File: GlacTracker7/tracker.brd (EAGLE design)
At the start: 120 x 89.3 mm, 84 parts, among them J1 THING_PLUS_PHYSICAL, Q1 2N3906, Q2 DMG6602SVT, Q3 DMG6602SVT, Q6 MMBT3906LT1SMD, Q7 DMG6602SVT, U2 FONA-800-BREAKOUT, U3 MP2155GQ-Z, U4 SPARKFUN-SWARM-M138, U5 SPARKFUN-GPS-ZED-F9P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

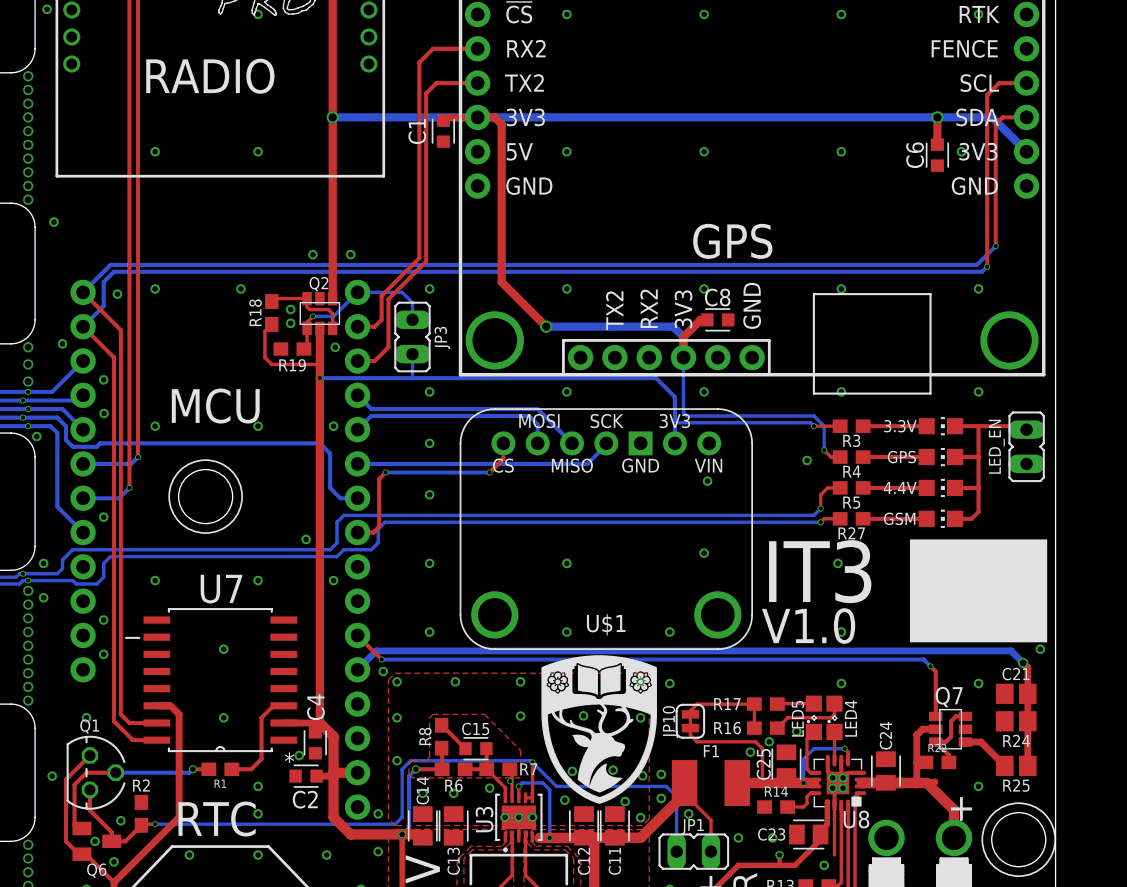
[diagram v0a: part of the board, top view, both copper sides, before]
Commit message: Added accelerometer
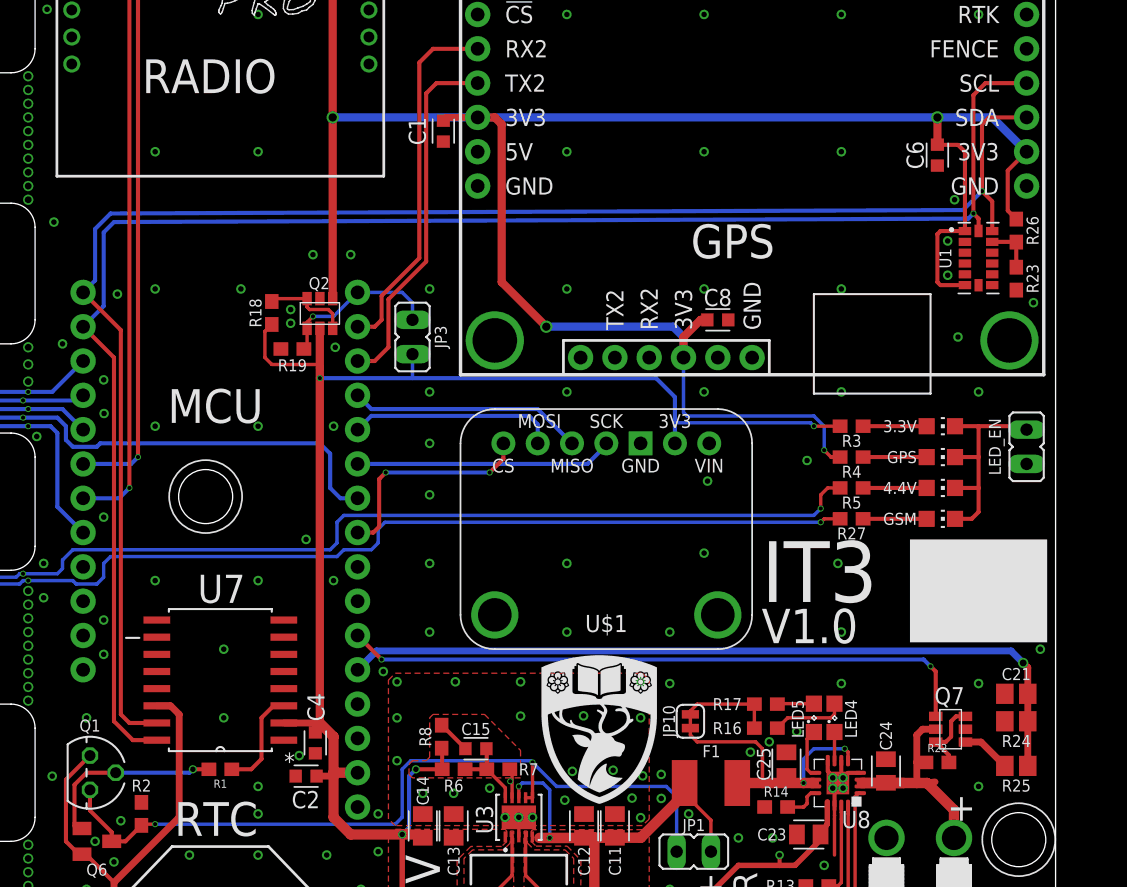
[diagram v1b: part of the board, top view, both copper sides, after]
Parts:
- added R23: 10k, SparkFun-Resistors:0603
- added R26: DNP, SparkFun-Resistors:0603
- added U1: ADXL343BCCZ-RL7, GlacTracker:PQFN80P300X500X100-14N
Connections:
- new net N$1: R23.2, R26.1, U1.12
- net GND: now also R23.1, U1.2, U1.4, U1.5
- net SCL: now also U1.14
- net SDA: now also U1.13
- net V_GPS: now also R26.2, U1.1, U1.6
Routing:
- net V_GPS: track 164.1 -> 185.8 mm
- net N$1: track 0.00 -> 3.65 mm
- net SDA: track 115.8 -> 118.8 mm
- net SCL: track 119.7 -> 120.9 mm
- net GND: vias 236 -> 239
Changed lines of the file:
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@@
 <setting verticaltext="up"/>
 </settings>
-<grid distance="0.4" unitdist="mil" unit="mil" style="lines" multiple="1" display="yes" altdistance="5" altunitdist="mil" altunit="mil"/>
+<grid distance="10" unitdist="mil" unit="mil" style="lines" multiple="1" display="yes" altdistance="5" altunitdist="mil" altunit="mil"/>
 <layers>
 <layer number="1" name="Top" color="4" fill="1" visible="yes" active="yes"/>
@@
 <attribute name="VALUE" x="90.678" y="7.493" size="1.27" layer="27" ratio="10"/>
 </element>
+<element name="U1" library="GlacTracker" package="PQFN80P300X500X100-14N" value="ADXL343BCCZ-RL7" x="114.3" y="54.356" smashed="yes">
+<attribute name="NAME" x="112.289" y="54.334" size="0.889" layer="25" rot="R90" align="bottom-center"/>
+<attribute name="VALUE" x="112.5" y="50.856" size="0.6096" layer="27"/>
+</element>
+<element name="R23" library="SparkFun-Resistors" package="0603" value="10k" x="117.094" y="52.832" smashed="yes" rot="R90">
+<attribute name="PROD_ID" value=" " x="117.094" y="52.832" size="0.02031875" layer="27" font="vector" rot="R90" display="off"/>
+<attribute name="NAME" x="117.856" y="52.832" size="0.889" layer="25" ratio="20" rot="R270" align="bottom-center"/>
+<attribute name="VALUE" x="117.856" y="52.832" size="0.6096" layer="27" font="vector" ratio="20" rot="R90" align="top-center"/>
+</element>
+<element name="R26" library="SparkFun-Resistors" package="0603" value="DNP" x="117.094" y="56.388" smashed="yes" rot="R90">
+<attribute name="PROD_ID" value=" " x="117.094" y="56.388" size="1.778" layer="27" rot="R90" display="off"/>
+<attribute name="NAME" x="117.856" y="56.388" size="0.889" layer="25" ratio="20" rot="R270" align="bottom-center"/>
+<attribute name="VALUE" x="117.856" y="56.388" size="0.6096" layer="27" font="vector" ratio="20" rot="R90" align="top-center"/>
+</element>
 </elements>
 <signals>
@@
 <via x="83.82" y="52.07" extent="1-16" drill="0.4064" diameter="0.7112"/>
 <via x="114.3" y="72.39" extent="1-16" drill="0.4064" diameter="0.7112"/>
-<via x="113.03" y="62.23" extent="1-16" drill="0.4064" diameter="0.7112"/>
-<via x="114.3" y="52.07" extent="1-16" drill="0.4064" diameter="0.7112"/>
+<via x="112.522" y="58.674" extent="1-16" drill="0.4064" diameter="0.7112"/>
+<via x="112.776" y="48.514" extent="1-16" drill="0.4064" diameter="0.7112"/>
 <via x="83.82" y="44.45" extent="1-16" drill="0.4064" diameter="0.7112"/>
 <via x="73.66" y="52.07" extent="1-16" drill="0.4064" diameter="0.7112"/>
@@
 <via x="75.438" y="14.732" extent="1-16" drill="0.4064" diameter="0.7112"/>
 <via x="83.6676" y="14.224" extent="1-16" drill="0.4064" diameter="0.7112"/>
-<via x="88.138" y="14.1224" extent="1-16" drill="0.4064" diameter="0.7112"/>
+<via x="88.646" y="14.3764" extent="1-16" drill="0.4064" diameter="0.7112"/>
 <via x="12.954" y="15.748" extent="1-16" drill="0.4064" diameter="0.7112"/>
 <via x="10.668" y="15.748" extent="1-16" drill="0.4064" diameter="0.7112"/>
@@
 <via x="50.292" y="9.652" extent="1-16" drill="0.4064" diameter="0.7112"/>
 <via x="48.895" y="11.176" extent="1-16" drill="0.4064" diameter="0.7112"/>
+<contactref element="U1" pad="4"/>
+<contactref element="U1" pad="5"/>
+<contactref element="U1" pad="2"/>
+<contactref element="R23" pad="1"/>
+<contactref element="U1" pad="4"/>
+<contactref element="U1" pad="5"/>
+<contactref element="U1" pad="2"/>
+<via x="112.014" y="55.626" extent="1-16" drill="0.4064" diameter="0.7112"/>
+<via x="112.014" y="53.086" extent="1-16" drill="0.4064" diameter="0.7112"/>
+<via x="118.364" y="51.054" extent="1-16" drill="0.4064" diameter="0.7112"/>
 </signal>
 <signal name="GPS_RX2">
@@
 <contactref element="U5" pad="12"/>
 <contactref element="U5" pad="23"/>
-<wire x1="50.038" y1="53.848" x2="48.006" y2="51.816" width="0.3048" layer="16"/>
 <wire x1="53.467" y1="19.939" x2="51.435" y2="19.939" width="0.3048" layer="1"/>
 <wire x1="51.435" y1="19.939" x2="50.8" y2="20.574" width="0.3048" layer="1"/>
 <wire x1="50.8" y1="20.574" x2="50.8" y2="49.022" width="0.3048" layer="1"/>
 <wire x1="50.8" y1="49.022" x2="48.006" y2="51.816" width="0.3048" layer="1"/>
-<wire x1="50.038" y1="53.848" x2="114.173" y2="53.848" width="0.3048" layer="16"/>
-<wire x1="114.173" y1="53.848" x2="115.57" y2="55.245" width="0.3048" layer="16"/>
-<via x="115.57" y="55.245" extent="1-16" drill="0.3048"/>
-<wire x1="115.57" y1="55.245" x2="115.57" y2="64.262" width="0.3048" layer="1"/>
-<wire x1="117.856" y1="64.77" x2="116.078" y2="64.77" width="0.3048" layer="1"/>
-<wire x1="116.078" y1="64.77" x2="115.57" y2="64.262" width="0.3048" layer="1"/>
-<wire x1="50.038" y1="53.848" x2="77.216" y2="72.39" width="0" layer="19" extent="16-16"/>
+<wire x1="50.038" y1="57.658" x2="113.157" y2="57.912" width="0.3048" layer="16"/>
+<wire x1="113.157" y1="57.912" x2="114.554" y2="59.309" width="0.3048" layer="16"/>
+<via x="114.554" y="59.309" extent="1-16" drill="0.3048"/>
+<wire x1="114.554" y1="59.309" x2="114.554" y2="64.262" width="0.3048" layer="1"/>
+<wire x1="117.856" y1="64.77" x2="115.062" y2="64.77" width="0.3048" layer="1"/>
+<wire x1="115.062" y1="64.77" x2="114.554" y2="64.262" width="0.3048" layer="1"/>
+<contactref element="U1" pad="13"/>
+<wire x1="50.038" y1="57.658" x2="48.895" y2="56.515" width="0.3048" layer="16"/>
+<wire x1="48.895" y1="56.515" x2="48.895" y2="52.705" width="0.3048" layer="16"/>
+<wire x1="48.895" y1="52.705" x2="48.006" y2="51.816" width="0.3048" layer="16"/>
+<wire x1="115.31" y1="56.356" x2="115.31" y2="58.553" width="0.3048" layer="1"/>
+<wire x1="115.31" y1="58.553" x2="114.554" y2="59.309" width="0.3048" layer="1"/>
+<wire x1="50.038" y1="57.658" x2="77.216" y2="72.39" width="0" layer="19" extent="16-16"/>
 </signal>
 <signal name="SCL">
@@
 <contactref element="U5" pad="22"/>
 <contactref element="U5" pad="15"/>
-<wire x1="50.292" y1="53.34" x2="49.53" y2="52.578" width="0.3048" layer="16"/>
-<wire x1="49.53" y1="52.578" x2="49.53" y2="50.8" width="0.3048" layer="16"/>
+<wire x1="50.292" y1="57.023" x2="49.53" y2="56.261" width="0.3048" layer="16"/>
+<wire x1="49.53" y1="56.261" x2="49.53" y2="50.8" width="0.3048" layer="16"/>
 <wire x1="49.53" y1="50.8" x2="48.006" y2="49.276" width="0.3048" layer="16"/>
 <wire x1="53.467" y1="18.669" x2="51.689" y2="18.669" width="0.3048" layer="1"/>
@@
 <wire x1="50.292" y1="20.066" x2="50.292" y2="46.99" width="0.3048" layer="1"/>
 <wire x1="50.292" y1="46.99" x2="48.006" y2="49.276" width="0.3048" layer="1"/>
-<wire x1="50.292" y1="53.34" x2="114.554" y2="53.34" width="0.3048" layer="16"/>
-<wire x1="114.554" y1="53.34" x2="114.935" y2="53.721" width="0.3048" layer="16"/>
-<via x="114.935" y="53.721" extent="1-16" drill="0.3048"/>
-<wire x1="114.935" y1="53.721" x2="114.935" y2="66.421" width="0.3048" layer="1"/>
-<wire x1="117.856" y1="67.31" x2="115.824" y2="67.31" width="0.3048" layer="1"/>
-<wire x1="115.824" y1="67.31" x2="114.935" y2="66.421" width="0.3048" layer="1"/>
-<wire x1="50.292" y1="53.34" x2="77.216" y2="80.01" width="0" layer="19" extent="16-16"/>
+<wire x1="50.292" y1="57.023" x2="113.538" y2="57.277" width="0.3048" layer="16"/>
+<wire x1="113.538" y1="57.277" x2="113.919" y2="57.658" width="0.3048" layer="16"/>
+<via x="113.919" y="57.658" extent="1-16" drill="0.3048"/>
+<wire x1="113.919" y1="57.658" x2="113.919" y2="66.421" width="0.3048" layer="1"/>
+<wire x1="117.856" y1="67.31" x2="114.808" y2="67.31" width="0.3048" layer="1"/>
+<wire x1="114.808" y1="67.31" x2="113.919" y2="66.421" width="0.3048" layer="1"/>
+<contactref element="U1" pad="14"/>
+<wire x1="114.3" y1="56.366" x2="114.3" y2="57.277" width="0.3048" layer="1"/>
+<wire x1="114.3" y1="57.277" x2="113.919" y2="57.658" width="0.3048" layer="1"/>
+<wire x1="50.292" y1="57.023" x2="77.216" y2="80.01" width="0" layer="19" extent="16-16"/>
 </signal>
 <signal name="COMMS_RX">
@@
 <wire x1="54.102" y1="81.28" x2="65.4698" y2="81.28" width="0.6096" layer="1"/>
 <wire x1="65.4698" y1="81.28" x2="66.4858" y2="80.264" width="0.6096" layer="1"/>
+<contactref element="U1" pad="1"/>
+<contactref element="U1" pad="6"/>
+<contactref element="R26" pad="2"/>
+<wire x1="113.29" y1="56.356" x2="113.29" y2="62.224" width="0.3048" layer="1"/>
+<wire x1="113.29" y1="62.224" x2="112.776" y2="62.738" width="0.3048" layer="1"/>
+<wire x1="112.776" y1="62.738" x2="111.2646" y2="62.738" width="0.3048" layer="1"/>
+<wire x1="111.2646" y1="62.738" x2="111.252" y2="62.7506" width="0.3048" layer="1"/>
+<wire x1="113.29" y1="56.356" x2="111.474" y2="56.356" width="0.3048" layer="1"/>
+<wire x1="111.474" y1="56.356" x2="111.252" y2="56.134" width="0.3048" layer="1"/>
+<wire x1="111.252" y1="56.134" x2="111.252" y2="52.578" width="0.3048" layer="1"/>
+<wire x1="111.252" y1="52.578" x2="111.474" y2="52.356" width="0.3048" layer="1"/>
+<wire x1="111.474" y1="52.356" x2="113.29" y2="52.356" width="0.3048" layer="1"/>
+<wire x1="117.094" y1="57.238" x2="116.459" y2="57.873" width="0.3048" layer="1"/>
+<wire x1="116.459" y1="57.873" x2="116.459" y2="60.833" width="0.3048" layer="1"/>
+<wire x1="116.459" y1="60.833" x2="117.856" y2="62.23" width="0.3048" layer="1"/>
 </signal>
 <signal name="N$35">
@@
 <contactref element="J1" pad="9"/>
 </signal>
+<signal name="N$1">
+<contactref element="U1" pad="12"/>
+<contactref element="R23" pad="2"/>
+<contactref element="R26" pad="1"/>
+<wire x1="115.31" y1="55.556" x2="117.076" y2="55.556" width="0.3048" layer="1"/>
+<wire x1="117.076" y1="55.556" x2="117.094" y2="55.538" width="0.3048" layer="1"/>
+<wire x1="117.094" y1="55.538" x2="117.094" y2="53.682" width="0.3048" layer="1"/>
+</signal>
 </signals>

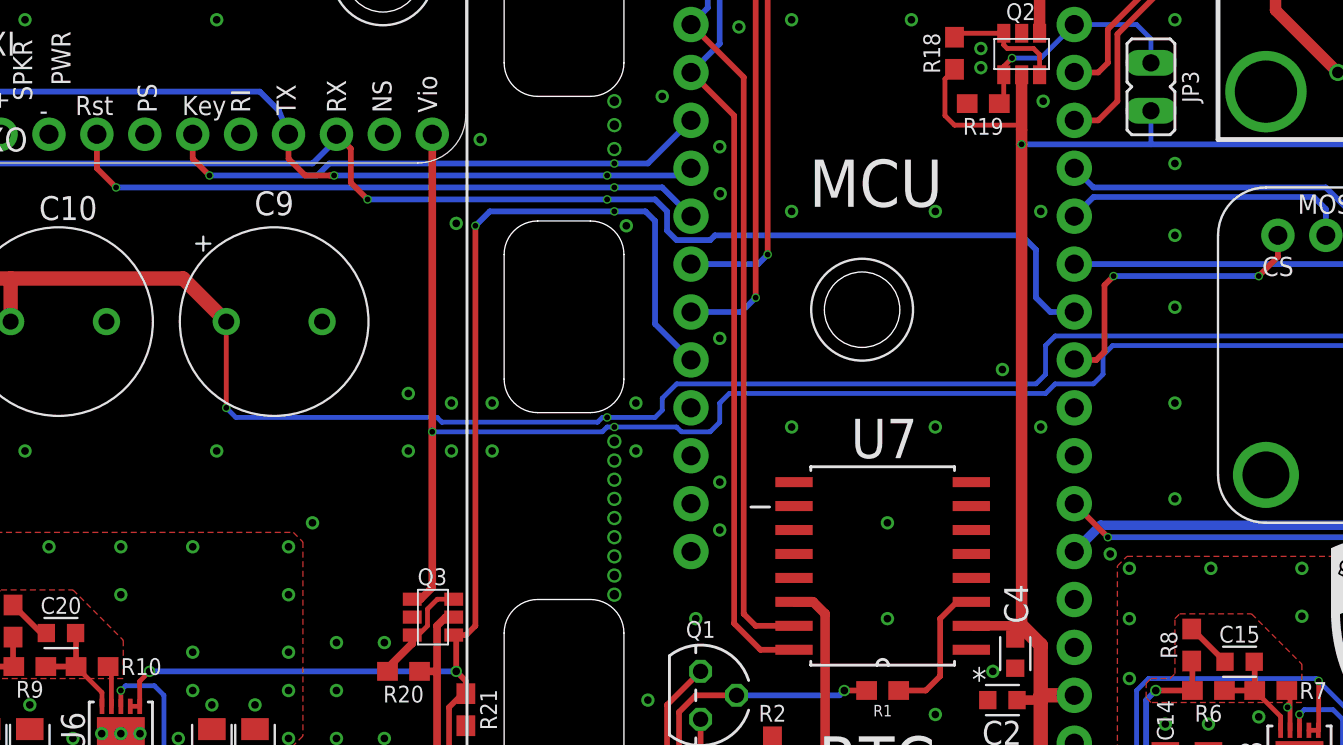
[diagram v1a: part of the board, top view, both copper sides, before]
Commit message: Change Key to be grounded and add an Admin pinheader for a button
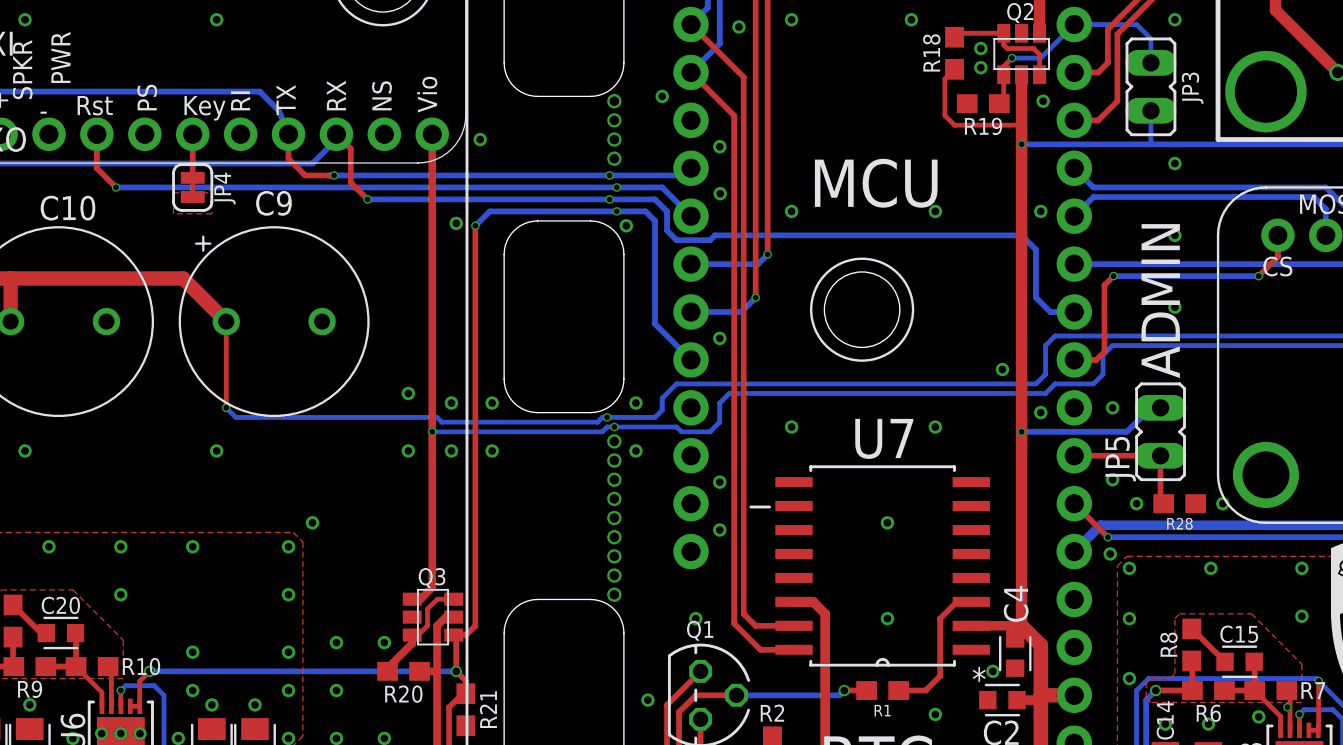
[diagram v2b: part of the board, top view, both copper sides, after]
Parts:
- added JP4: JUMPER-SMT_2_NC_TRACE_SILK, SparkFun-Jumpers:SMT-JUMPER_2_NC_TRACE_SILK
- added JP5: (no value), jumper:JP1
- added R28: 10k, SparkFun-Resistors:0603
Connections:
- removed net SPARE3: J1.22
- new net ADMIN: J1.22, JP5.1, R28.2
- new net SPARE1: J1.3
- net 3.3V: now also JP5.2
- net GND: now also JP4.2, R28.1
- net GSM_KEY: now also JP4.1; no longer J1.3
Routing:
- net GSM_KEY: track 29.3 -> 2.31 mm, vias 2 -> 0
- net 3.3V: track 185.0 -> 192.9 mm, vias 8 -> 9
- net ADMIN: track 0.00 -> 7.14 mm
- net GND: vias 239 -> 242
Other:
- board text added: "ADMIN"

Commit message: Fix the overlapping holes DRC
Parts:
- added U$2: SLOT130.5, GlacTracker:SLOT130.5
- U2: value FONA-800-BREAKOUT -> FONA-800-BREAKOUTNOHOLE; device GlacTracker:FONA-800-BREAKOUT -> GlacTracker:FONA-800-BREAKOUT-NH
- U4: value SPARKFUN-SWARM-M138 -> SPARKFUN-SWARM-M138NOTOPHOLE; device GlacTracker:SPARKFUN-SWARM-M138 -> GlacTracker:SPARKFUN-SWARM-M138-NTH
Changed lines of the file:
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@@
 <setting verticaltext="up"/>
 </settings>
-<grid distance="10" unitdist="mil" unit="mil" style="lines" multiple="1" display="yes" altdistance="5" altunitdist="mil" altunit="mil"/>
+<grid distance="10" unitdist="mil" unit="mil" style="lines" multiple="1" display="yes" altdistance="0.5" altunitdist="mil" altunit="mil"/>
 <layers>
 <layer number="1" name="Top" color="4" fill="1" visible="yes" active="yes"/>
@@
 <layer number="42" name="bRestrict" color="1" fill="10" visible="no" active="yes"/>
 <layer number="43" name="vRestrict" color="2" fill="10" visible="no" active="yes"/>
-<layer number="44" name="Drills" color="7" fill="1" visible="no" active="yes"/>
-<layer number="45" name="Holes" color="7" fill="1" visible="no" active="yes"/>
-<layer number="46" name="Milling" color="3" fill="1" visible="no" active="yes"/>
+<layer number="44" name="Drills" color="7" fill="1" visible="yes" active="yes"/>
+<layer number="45" name="Holes" color="7" fill="1" visible="yes" active="yes"/>
+<layer number="46" name="Milling" color="3" fill="1" visible="yes" active="yes"/>
 <layer number="47" name="Measures" color="7" fill="1" visible="no" active="yes"/>
 <layer number="48" name="Document" color="7" fill="1" visible="no" active="yes"/>
@@
 </autorouter>
 <elements>
-<element name="U4" library="GlacTracker" package="SPARKFUN-SWARM-M138" value="SPARKFUN-SWARM-M138" x="0.508" y="0" smashed="yes"/>
+<element name="U4" library="GlacTracker" package="SPARKFUN-SWARM-M138-NTH" value="SPARKFUN-SWARM-M138NOTOPHOLE" x="0.508" y="0" smashed="yes"/>
 <element name="U5" library="GlacTracker" package="SPARKFUN-GPS-ZED-F9P" value="SPARKFUN-GPS-ZED-F9P" x="119.126" y="45.72" smashed="yes" rot="R90"/>
 <element name="J1" library="SparkFun-Boards" package="THING_PLUS" value="THING_PLUS_PHYSICAL" x="46.736" y="-0.254" smashed="yes">
@@
 <attribute name="VOLTAGE_RATING" value="" x="50.038" y="84.017" size="1.778" layer="27" rot="R270" display="off"/>
 </element>
-<element name="U2" library="GlacTracker" package="FONA-800-BREAKOUT" value="FONA-800-BREAKOUT" x="4.318" y="44.4754" smashed="yes"/>
+<element name="U2" library="GlacTracker" package="FONA-800-BREAKOUT-NH" value="FONA-800-BREAKOUTNOHOLE" x="4.318" y="44.4754" smashed="yes"/>
 <element name="Q1" library="transistor-pnp" package="TO92" value="2N3906" x="48.514" y="16.256" smashed="yes" rot="R270">
 <attribute name="NAME" x="48.514" y="19.304" size="0.889" layer="25" ratio="10" align="bottom-center"/>
@@
 <attribute name="VALUE" x="73.914" y="27.178" size="0.6096" layer="27" font="vector" ratio="20" rot="R180" align="top-center"/>
 </element>
+<element name="U$2" library="GlacTracker" package="SLOT130.5" value="SLOT130.5" x="5.0038" y="86.3854"/>
 </elements>
 <signals>
@@
 <contactref element="J1" pad="3"/>
 </signal>
+<signal name="N$6">
+<via x="33.528" y="86.3727" extent="1-16" drill="3.3147"/>
+</signal>
 </signals>
